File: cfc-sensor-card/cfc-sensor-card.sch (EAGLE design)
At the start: 138 parts, among them J2 J-SAMTEC-TFM-110-X1-XXX-D-RA, J4 TFM-120-01-L-D-RA, Q1 35A/25V/8.5mΩ, Q2 PMV45EN, Q3 DMP2240UDM, Q4 PMV45EN, Q5 MOSFET-PCH-SOT23-6, Q6 MOSFET-PCH-SOT23-6, U1 PIRT1280A1-12, U12 MIC842LYC5, U13 MIC842LYC5, U14 MAX4211FETE, U16 MAX7310ATE, U2 LT3042IMSE#TRPBF, U3 LT3042IMSE#TRPBF, U4 LT3042IMSE#TRPBF, U5 LT3042IMSE#TRPBF, U6 LT3042IMSE#TRPBF, U7 TLC3704IPWRPW14-M, X1 16MHz

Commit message: mostly finished sensor card
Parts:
- removed R21: 1k, oresat-rcl:R-US_0603-A
- removed TP65, TP66: TEST-POINT_SMD-SMD-10SN, oresat-misc:TEST-POINT_SMD-SMD-10SN
- added C18: 1uF, oresat-rcl:C-EU0603-B
- added C19: 4.7u, oresat-rcl:C-EU0603-B
- added C20: 0.1u, oresat-rcl:C-EU0603-B
- added D2: GREEN, SparkFun-LED:LED-GREEN0603
- added Q7: MOSFET-PCH-SOT23-6, Q-MOSFET-PCH-SOT23-6:MOSFET-PCH-SOT23-6
- added Q8: PMV45EN, Tova:PMV45EN
- added R10, R8, R9: 10k, oresat-rcl:R-US_0603-B
- added R11: 1k, oresat-rcl:R-US_0603-B
- added U8: LP2985AIM5-3.3_NOPB, U-TI-LP2985AIM5-3.3_NOPB-3.3V-Fixed-LDO:LP2985AIM5-3.3_NOPB
- C1, C10, C11, C12, C13, C14, C15, C16, C17, C2, C3, C4, C5, C6, C7, C8, C9: device oresat-rcl:C-EU0603-A -> oresat-rcl:C-EU0603-B
- C40: value 0.1u -> 1u; device oresat-rcl:C-EU0603-A -> oresat-rcl:C-EU0603-B
- Q1: value 35A/25V/8.5mΩ -> MOSFET-PCH-SOT23-6; device Q-Fairchild-FDD8780-MOSFET-NCH:MOSFET-NCH-FDD8780 -> Q-MOSFET-PCH-SOT23-6:MOSFET-PCH-SOT23-6; MPN (none) -> DMP3050LVT-7
- R1, R3, R4, R5, R6, R7: device oresat-rcl:R-US_0603-A -> oresat-rcl:R-US_0603-B
- R18: device oresat-rcl:R-US_0805-A -> oresat-rcl:R-US_0603-B
- R19: value 20k -> 10k; device oresat-rcl:R-US_0805-A -> oresat-rcl:R-US_0603-B
- R27: device oresat-rcl:R-US_0402-C-NOSILK -> oresat-rcl:R-US_0402-A
- TP40: value TEST-POINT-LARGE-SQUARE -> TEST-POINT_SMD-SMD-10SN; device oresat-misc:TEST-POINT-LARGE-SQUARE -> oresat-misc:TEST-POINT_SMD-SMD-10SN
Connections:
- removed net N$19: Q1.D, U1G$1.TEC-
- removed net N$30: Q1.S, R21.2
- new net N$12: D2.A, R11.1
- new net N$18: C20.1, U8.BYPASS
- new net N$2: R19.1, R8.2
- new net N$3: Q1.G, Q7.G, Q8.D, R9.1
- new net TEC+: Q1.D, Q7.D, R11.2, U1G$1.TEC+
- net 3.3V: now also C19.1, U8.VOUT
- net GND: now also C18.2, C19.2, C20.2, D2.C, Q8.S, R10.1, U1G$1.TEC-, U8.GND
- net OUT1N: now also J2.5, J2.6; no longer J2.1, J2.2
- net OUT1P: now also J2.7, J2.8; no longer J2.3, J2.4
- net PEN-SCL-FILT: no longer TP66.1
- net PEN-SDA-FILT: no longer TP65.1
- net SENSOR_ENABLE: now also R8.1; no longer R19.1
- net TEC_ENABLE: now also Q8.G, R10.2; no longer Q1.G, R20.22, R21.1
- net TXCLKN: now also J2.1, J2.2; no longer J2.5, J2.6
- net TXCLKP: now also J2.3, J2.4; no longer J2.7, J2.8
- net VBUSP: now also C18.1, Q1.S, Q7.S, R9.2, U8.EN, U8.VIN; no longer U1G$1.TEC+
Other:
- note added: "10k + 10k == 20k"
- note added: "2 High-side P-Channel MOSFETs driven by single N-Channel MOSFET"
- note added: "Card 3.3V LDO"
- note added: "TEC Drive Circuit"
- note removed: "TODO Anything between VBUSP and TEC?"
- note removed: "TODO multiple, flatter, mosfets"

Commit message: mostly finished octavo card
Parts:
- removed Q1: MOSFET-PCH-SOT23-6, Q-MOSFET-PCH-SOT23-6:MOSFET-PCH-SOT23-6
- R2: device R-Panasonic-EXB-2HV103JV:EXB-2HV103JV -> R-Panasonic-EXB-2HV103JV:EXB-2HV103JV-LEGACY
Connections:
- net N$3: no longer Q1.G
- net TEC+: no longer Q1.D
- net VBUSP: no longer Q1.S
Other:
- note added: "High-side P-Channel MOSFET driven by N-Channel MOSFET"
- note removed: "2 High-side P-Channel MOSFETs driven by single N-Channel MOSFET"
- moved on the sheet: D2, Q8, R10, R11, R9

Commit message: boards finished
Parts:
- added C21: NP, oresat-rcl:C-EU0603-B
- added R12, R13, R14: NP, oresat-rcl:R-US_0402-C-NOSILK
- added R15: 0, oresat-rcl:R-US_0603-B
- C100, C101, C102, C103, C104: device oresat-rcl:C-EU0805-A -> oresat-rcl:C-EU0603-B
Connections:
- new net N$11: R12.2, U1G$1.OUT2P
- new net N$19: R12.1, U1G$1.OUT2N
- new net N$21: R13.2, U1G$1.OUT3P
- new net N$22: R13.1, U1G$1.OUT3N
- new net N$26: R14.2, U1G$1.OUT4P
- new net N$30: R14.1, U1G$1.OUT4N
- new net N$31: Q8.D, R15.1
- net N$3: now also C21.2, R15.2; no longer Q8.D
- net VBUSP: now also C21.1
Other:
- note added: "NOTE: R15 and C21 for a possible slow start circuit if needed"
- note added: "TODO CALCULATE ACTUAL CURRENT LIMIT RES VALUES"
- moved on the sheet: D2, Q7, Q8, R10, R11

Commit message: update attrs
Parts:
- C100, C101, C102, C103, C104: value 100n -> 0.1u
- C18, C32, C34, C35: value 1uF -> 1u
- C33: value 1uF -> 1u; DIS Digi-Key -> (none); DPN 1276-1001-1-ND -> (none); MFR Samsung -> (none); MPN CL05B104KO5NNNC -> (none)
- C39: value 0.1uF -> 0.1u
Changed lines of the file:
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@@
 </part>
 <part name="GND9" library="supply1" library_urn="urn:adsk.eagle:library:371" deviceset="GND" device=""/>
-<part name="C39" library="oresat-rcl" deviceset="C-EU" device="0603-B" value="0.1uF"/>
+<part name="C39" library="oresat-rcl" deviceset="C-EU" device="0603-B" value="0.1u"/>
 <part name="GND12" library="supply1" library_urn="urn:adsk.eagle:library:371" deviceset="GND" device=""/>
 <part name="R71" library="oresat-rcl" deviceset="R-US_" device="0603-B" value="100"/>
@@
 </part>
 <part name="GND21" library="supply1" library_urn="urn:adsk.eagle:library:371" deviceset="GND" device=""/>
-<part name="C33" library="oresat-rcl" deviceset="C-EU" device="0603-B" value="1uF">
-<attribute name="DIS" value="Digi-Key"/>
-<attribute name="DPN" value="1276-1001-1-ND"/>
-<attribute name="MFR" value="Samsung"/>
-<attribute name="MPN" value="CL05B104KO5NNNC"/>
-</part>
+<part name="C33" library="oresat-rcl" deviceset="C-EU" device="0603-B" value="1u"/>
 <part name="GND28" library="supply1" library_urn="urn:adsk.eagle:library:371" deviceset="GND" device=""/>
 <part name="R32" library="oresat-rcl" deviceset="R-US_" device="0603-B" value="10k"/>
@@
 <attribute name="MPN" value="PMV45EN2R"/>
 </part>
-<part name="C34" library="oresat-rcl" deviceset="C-EU" device="0603-B" value="1uF"/>
+<part name="C34" library="oresat-rcl" deviceset="C-EU" device="0603-B" value="1u"/>
 <part name="GND20" library="supply1" library_urn="urn:adsk.eagle:library:371" deviceset="GND" device=""/>
 <part name="VBUSP2" library="oresat-supplies" deviceset="VBUSP" device=""/>
@@
 <part name="GND11" library="supply1" library_urn="urn:adsk.eagle:library:371" deviceset="GND" device=""/>
 <part name="VPD4" library="oresat-supplies" deviceset="VPD" device=""/>
-<part name="C35" library="oresat-rcl" deviceset="C-EU" device="0603-B" value="1uF"/>
+<part name="C35" library="oresat-rcl" deviceset="C-EU" device="0603-B" value="1u"/>
 <part name="GND8" library="supply1" library_urn="urn:adsk.eagle:library:371" deviceset="GND" device=""/>
 <part name="TP41" library="oresat-misc" deviceset="TEST-POINT_SMD" device="-SMD-10SN" package3d_urn="urn:adsk.eagle:package:15662280/2"/>
@@
 <part name="GND10" library="supply1" library_urn="urn:adsk.eagle:library:371" deviceset="GND" device=""/>
 <part name="VPD3" library="oresat-supplies" deviceset="VPD" device=""/>
-<part name="C32" library="oresat-rcl" deviceset="C-EU" device="0603-B" value="1uF"/>
+<part name="C32" library="oresat-rcl" deviceset="C-EU" device="0603-B" value="1u"/>
 <part name="GND7" library="supply1" library_urn="urn:adsk.eagle:library:371" deviceset="GND" device=""/>
 <part name="TP42" library="oresat-misc" deviceset="TEST-POINT_SMD" device="-SMD-10SN" package3d_urn="urn:adsk.eagle:package:15662280/2"/>
@@
 <part name="GND56" library="supply" deviceset="GND" device=""/>
 <part name="GND58" library="supply" deviceset="GND" device=""/>
-<part name="C103" library="oresat-rcl" deviceset="C-EU" device="0603-B" value="100n"/>
-<part name="C100" library="oresat-rcl" deviceset="C-EU" device="0603-B" value="100n"/>
-<part name="C102" library="oresat-rcl" deviceset="C-EU" device="0603-B" value="100n"/>
-<part name="C101" library="oresat-rcl" deviceset="C-EU" device="0603-B" value="100n"/>
-<part name="C104" library="oresat-rcl" deviceset="C-EU" device="0603-B" value="100n"/>
+<part name="C103" library="oresat-rcl" deviceset="C-EU" device="0603-B" value="0.1u"/>
+<part name="C100" library="oresat-rcl" deviceset="C-EU" device="0603-B" value="0.1u"/>
+<part name="C102" library="oresat-rcl" deviceset="C-EU" device="0603-B" value="0.1u"/>
+<part name="C101" library="oresat-rcl" deviceset="C-EU" device="0603-B" value="0.1u"/>
+<part name="C104" library="oresat-rcl" deviceset="C-EU" device="0603-B" value="0.1u"/>
 <part name="GND57" library="supply" deviceset="GND" device=""/>
 <part name="TP1" library="oresat-misc" deviceset="TEST-POINT-LARGE-SQUARE" device=""/>
@@
 <part name="3.3V3" library="oresat-supplies" deviceset="3.3V" device=""/>
 <part name="GND62" library="supply1" library_urn="urn:adsk.eagle:library:371" deviceset="GND" device=""/>
-<part name="C18" library="oresat-rcl" deviceset="C-EU" device="0603-B" value="1uF"/>
+<part name="C18" library="oresat-rcl" deviceset="C-EU" device="0603-B" value="1u"/>
 <part name="C19" library="oresat-rcl" deviceset="C-EU" device="0603-B" value="4.7u"/>
 <part name="VBUSP8" library="oresat-supplies" deviceset="VBUSP" device=""/>
@@
 </instance>
 <instance part="C33" gate="CE" x="273.05" y="224.79" smashed="yes" rot="MR180">
-<attribute name="DIS" x="273.05" y="224.79" size="1.778" layer="96" rot="MR180" display="off"/>
-<attribute name="DPN" x="273.05" y="224.79" size="1.778" layer="96" rot="MR180" display="off"/>
-<attribute name="MFR" x="273.05" y="224.79" size="1.778" layer="96" rot="MR180" display="off"/>
-<attribute name="MPN" x="273.05" y="224.79" size="1.778" layer="96" rot="MR180" display="off"/>
 <attribute name="NAME" x="276.86" y="226.06" size="1.778" layer="95"/>
 <attribute name="VALUE" x="275.59" y="223.52" size="1.778" layer="96"/>

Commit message: Fixed R27 attributes, and fixed names layer
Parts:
- R27: DIS Dgi-Key -> Digi-Key; DPN 311-100MCT-ND -> 541-3239-1-ND; MFR Yageo -> Vishay; MPN RC0201FR-07100RL -> RCA0402100RFKEDHP
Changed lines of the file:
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@@
 <?xml version="1.0" encoding="utf-8"?>
 <!DOCTYPE eagle SYSTEM "eagle.dtd">
-<eagle version="9.6.2">
+<eagle version="9.5.1">
 <drawing>
 <settings>
@@
 <part name="GND52" library="oresat-supplies" deviceset="GND" device=""/>
 <part name="R27" library="oresat-rcl" deviceset="R-US_" device="0402-A" value="100">
-<attribute name="DIS" value="Dgi-Key"/>
-<attribute name="DPN" value="311-100MCT-ND"/>
-<attribute name="MFR" value="Yageo"/>
-<attribute name="MPN" value="RC0201FR-07100RL"/>
+<attribute name="DIS" value="Digi-Key"/>
+<attribute name="DPN" value="541-3239-1-ND"/>
+<attribute name="MFR" value="Vishay"/>
+<attribute name="MPN" value="RCA0402100RFKEDHP"/>
 </part>
 <part name="C11" library="oresat-rcl" deviceset="C-EU" device="0603-B" value="0.1u"/>

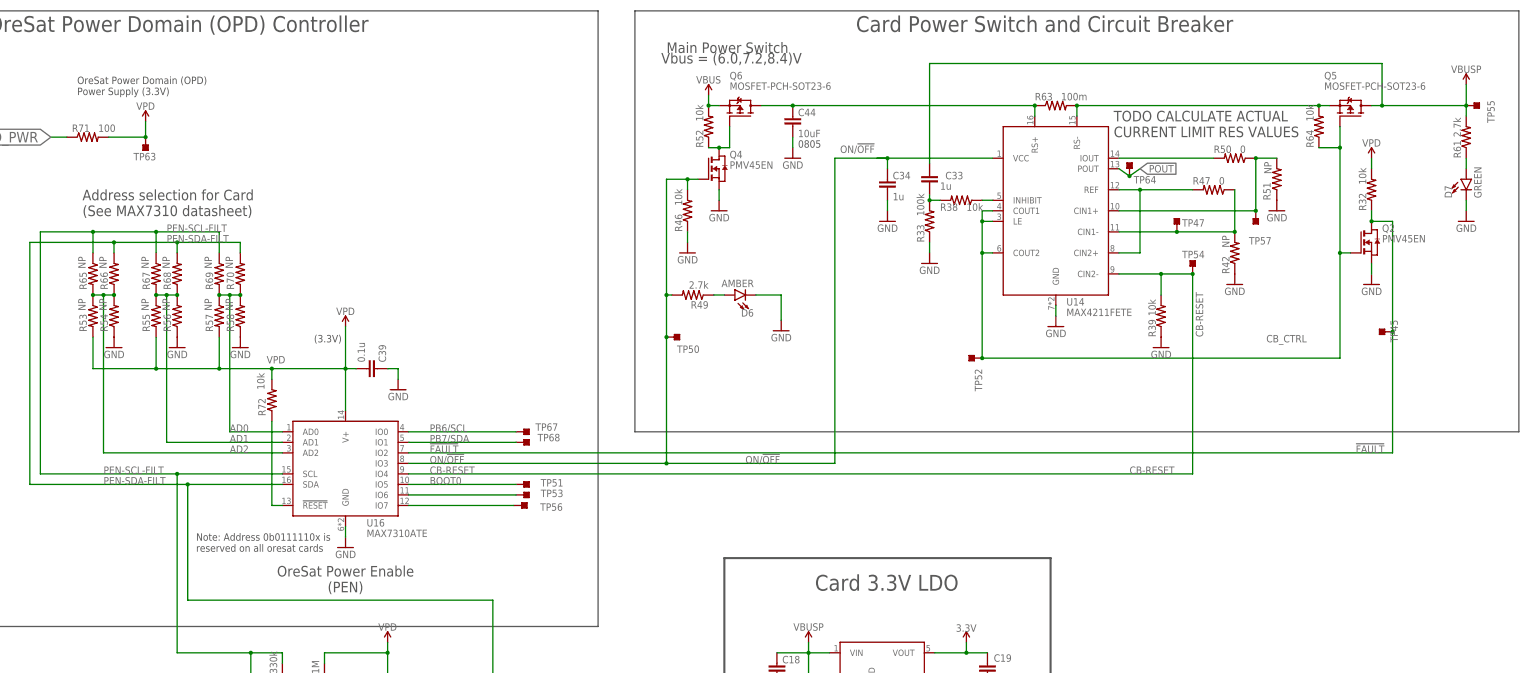
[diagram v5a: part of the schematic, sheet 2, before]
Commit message: Updated OPD address resistors, LED resistors (AAAAAUGH MY EYES), and OPD shunt resistor to give the CFC sensor card addrss 0x1E and a 2.95 A current limit.
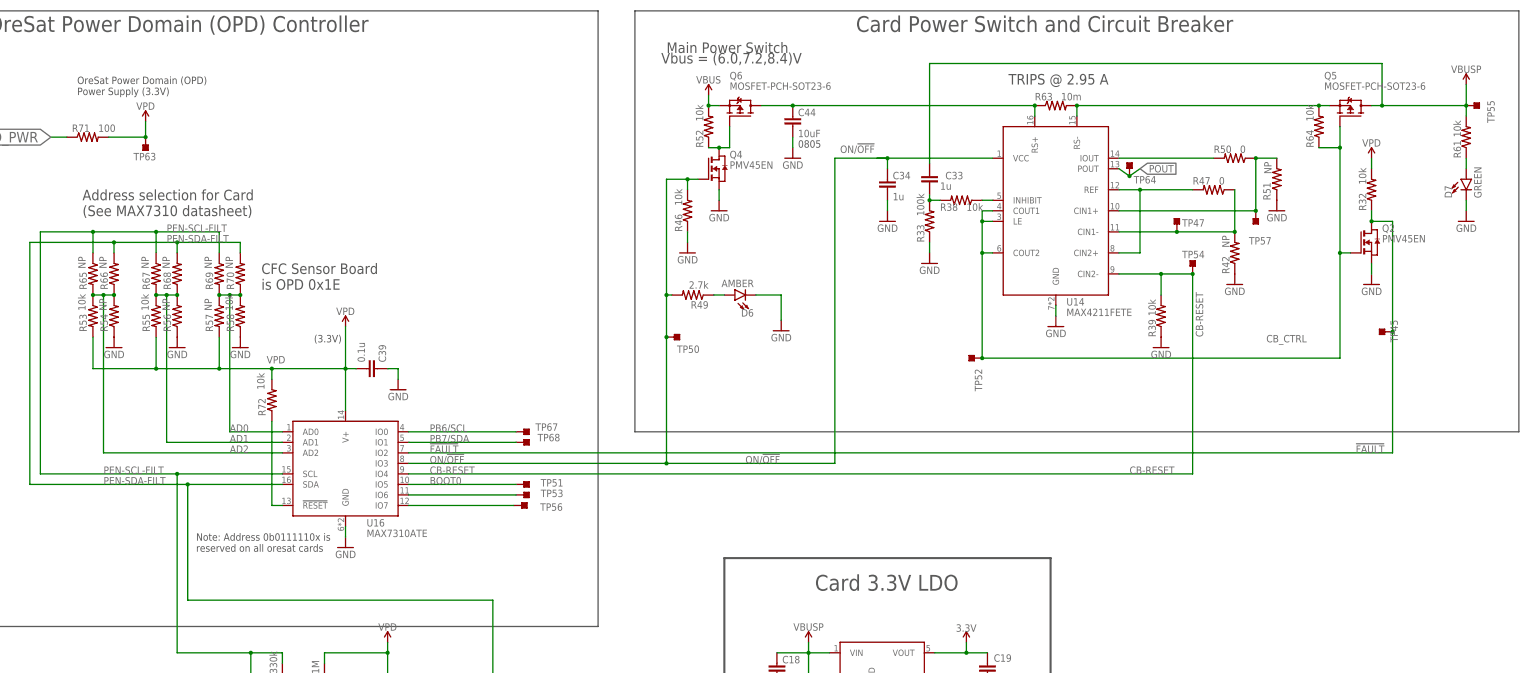
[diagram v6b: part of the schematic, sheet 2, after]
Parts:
- R1: value 1k -> 2.7k
- R11: value 1k -> 10k
- R53, R55, R58: value NP -> 10k
- R61: value 2.7k -> 10k
- R63: value 100m -> 10m
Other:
- note added: "CFC Sensor Board is OPD 0x1E"
- note added: "TRIPS @ 2.95 A"
- note removed: "OreSat Power Enable (PEN)"
- note removed: "TODO CALCULATE ACTUAL CURRENT LIMIT RES VALUES"
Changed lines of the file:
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@@
 <?xml version="1.0" encoding="utf-8"?>
 <!DOCTYPE eagle SYSTEM "eagle.dtd">
-<eagle version="9.5.1">
+<eagle version="9.6.2">
 <drawing>
 <settings>
@@
 <part name="D7" library="SparkFun-LED" deviceset="LED-GREEN" device="0603" value="GREEN"/>
 <part name="GND29" library="supply1" library_urn="urn:adsk.eagle:library:371" deviceset="GND" device=""/>
-<part name="R61" library="oresat-rcl" deviceset="R-US_" device="0603-B" value="2.7k"/>
+<part name="R61" library="oresat-rcl" deviceset="R-US_" device="0603-B" value="10k"/>
 <part name="J4" library="J-Samtec-TFM-120-X1-XXX-D-RA" deviceset="J-SAMTEC-TFM-120-X1-XXX-D-RA" device="" value="TFM-120-01-L-D-RA"/>
 <part name="GND1" library="supply1" library_urn="urn:adsk.eagle:library:371" deviceset="GND" device=""/>
@@
 <attribute name="MPN" value="RC1005F6653CS"/>
 </part>
-<part name="R58" library="oresat-rcl" deviceset="R-US_" device="0603-B" value="NP">
+<part name="R58" library="oresat-rcl" deviceset="R-US_" device="0603-B" value="10k">
 <attribute name="DIS" value="Digi-Key"/>
 <attribute name="DPN" value="1276-4275-1-ND"/>
@@
 </part>
 <part name="GND6" library="supply1" library_urn="urn:adsk.eagle:library:371" deviceset="GND" device=""/>
-<part name="R55" library="oresat-rcl" deviceset="R-US_" device="0603-B" value="NP">
+<part name="R55" library="oresat-rcl" deviceset="R-US_" device="0603-B" value="10k">
 <attribute name="DIS" value="Digi-Key"/>
 <attribute name="DPN" value="1276-4275-1-ND"/>
@@
 </part>
 <part name="GND3" library="supply1" library_urn="urn:adsk.eagle:library:371" deviceset="GND" device=""/>
-<part name="R53" library="oresat-rcl" deviceset="R-US_" device="0603-B" value="NP">
+<part name="R53" library="oresat-rcl" deviceset="R-US_" device="0603-B" value="10k">
 <attribute name="DIS" value="Digi-Key"/>
 <attribute name="DPN" value="1276-4275-1-ND"/>
@@
 <part name="R46" library="oresat-rcl" deviceset="R-US_" device="0603-B" value="10k"/>
 <part name="GND15" library="supply1" library_urn="urn:adsk.eagle:library:371" deviceset="GND" device=""/>
-<part name="R63" library="rcl" library_urn="urn:adsk.eagle:library:334" deviceset="R-US_" device="R1206" package3d_urn="urn:adsk.eagle:package:23540/2" value="100m"/>
+<part name="R63" library="rcl" library_urn="urn:adsk.eagle:library:334" deviceset="R-US_" device="R1206" package3d_urn="urn:adsk.eagle:package:23540/2" value="10m"/>
 <part name="R39" library="oresat-rcl" deviceset="R-US_" device="0603-B" value="10k"/>
 <part name="GND25" library="supply1" library_urn="urn:adsk.eagle:library:371" deviceset="GND" device=""/>
@@
 </part>
 <part name="GND53" library="supply1" library_urn="urn:adsk.eagle:library:371" deviceset="GND" device=""/>
-<part name="R1" library="oresat-rcl" deviceset="R-US_" device="0603-B" value="1k"/>
+<part name="R1" library="oresat-rcl" deviceset="R-US_" device="0603-B" value="2.7k"/>
 <part name="C40" library="oresat-rcl" deviceset="C-EU" device="0603-B" value="1u"/>
 <part name="GND55" library="supply" deviceset="GND" device=""/>
@@
 </part>
 <part name="GND63" library="supply1" library_urn="urn:adsk.eagle:library:371" deviceset="GND" device=""/>
-<part name="R11" library="oresat-rcl" deviceset="R-US_" device="0603-B" value="1k"/>
+<part name="R11" library="oresat-rcl" deviceset="R-US_" device="0603-B" value="10k"/>
 <part name="R12" library="oresat-rcl" deviceset="R-US_" device="0402-C-NOSILK" value="NP">
 <attribute name="DIS" value="Dgi-Key"/>
@@
 <text x="416.56" y="6.35" size="3.81" layer="94">1.2</text>
 <text x="209.55" y="256.54" size="2.54" layer="97">Main Power Switch</text>
-<text x="132.08" y="129.54" size="2.54" layer="97" align="center">OreSat Power Enable
-(PEN)</text>
 <text x="68.58" y="217.17" size="2.54" layer="97">Address selection for Card
 (See MAX7310 datasheet)</text>
@@
 <wire x1="302.26" y1="78.74" x2="302.26" y2="134.62" width="0.508" layer="97"/>
 <wire x1="302.26" y1="134.62" x2="223.52" y2="134.62" width="0.508" layer="97"/>
-<text x="317.5" y="236.22" size="2.54" layer="97">TODO CALCULATE ACTUAL
-CURRENT LIMIT RES VALUES</text>
+<text x="292.1" y="248.92" size="2.54" layer="97">TRIPS @ 2.95 A</text>
+<text x="111.76" y="199.39" size="2.54" layer="97">CFC Sensor Board
+is OPD 0x1E</text>
 </plain>
 <instances>
